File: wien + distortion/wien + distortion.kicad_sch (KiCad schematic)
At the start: 46 parts, among them J1 INPUT, J1 OUTPUT, J2 OUTPUT, J2 PWR switch, J5 Conn_01x01_Pin, U1 NE5532, U4 NE5532, U5 NE5532

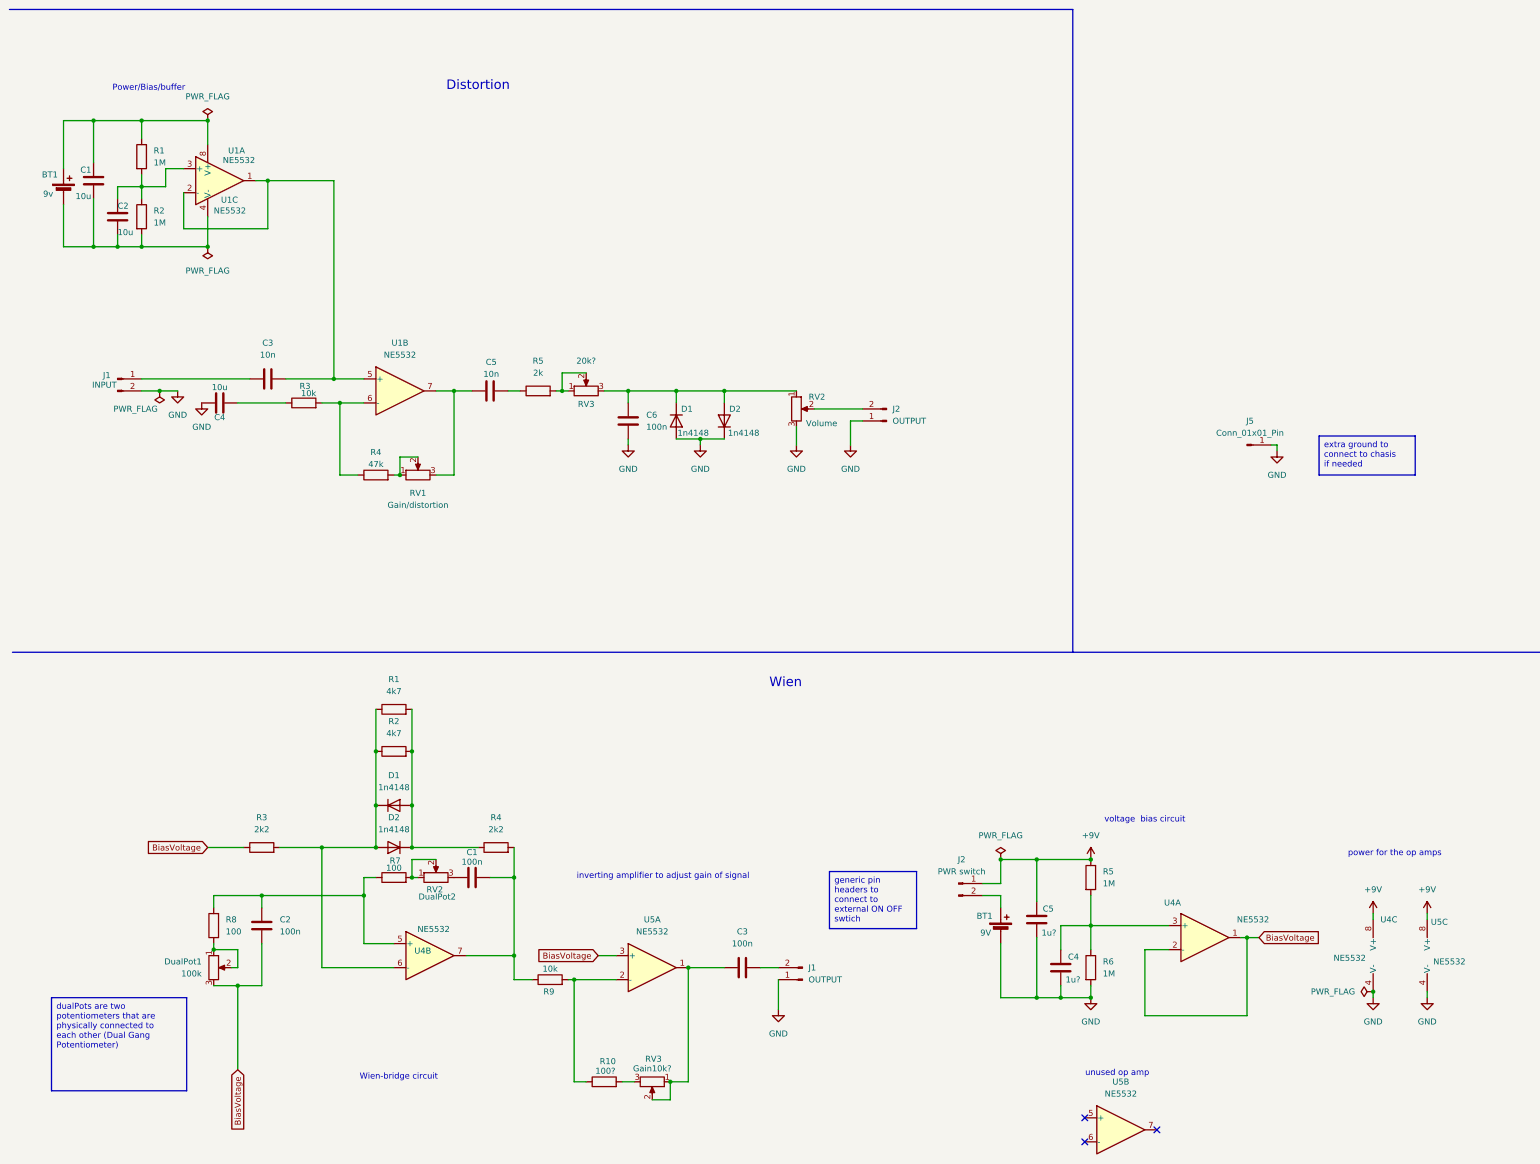
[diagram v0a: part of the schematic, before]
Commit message: decided to use one power supply for both circuits so redid the pcb to reflect that
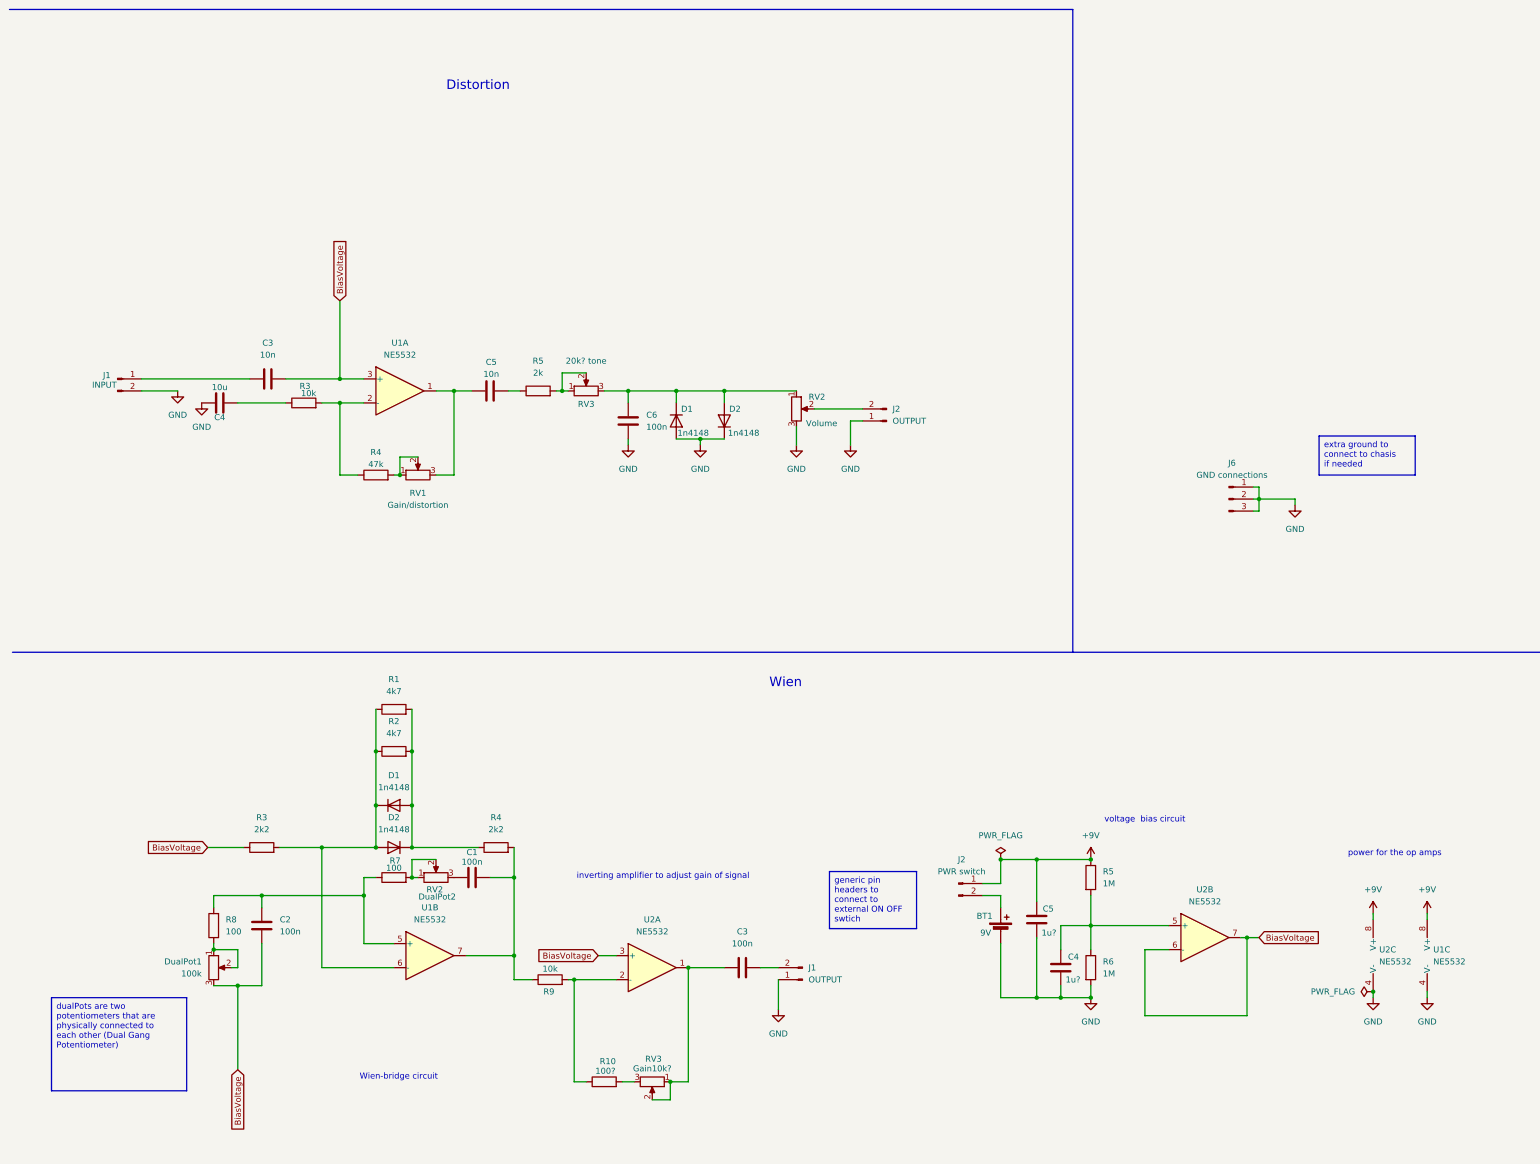
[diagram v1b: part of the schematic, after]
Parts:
- removed BT1: 9v, Connector_PinHeader_2.54mm:PinHeader_1x02_P2.54mm_Vertical, symbol Device:Battery_Cell
- removed C1, C2: 10u, Capacitor_SMD:C_0603_1608Metric_Pad1.08x0.95mm_HandSolder, symbol Device:C
- removed J5: Conn_01x01_Pin, Connector_PinHeader_2.54mm:PinHeader_1x01_P2.54mm_Vertical, symbol Connector:Conn_01x01_Pin
- removed R1, R2: 1M, Resistor_SMD:R_0603_1608Metric_Pad0.98x0.95mm_HandSolder, symbol Device:R
- removed U4, U5: NE5532, Package_DIP:DIP-8_W7.62mm, symbol Amplifier_Operational:NE5532
- added J6: GND connections, Connector_PinHeader_2.54mm:PinHeader_1x03_P2.54mm_Vertical, symbol Connector:Conn_01x03_Pin
- added U2: NE5532, Package_DIP:DIP-8_W7.62mm_LongPads, symbol Amplifier_Operational:NE5532
- RV3: value 20k? -> 20k? tone
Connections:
- net +9V: now also U1.8 (V+), U2.8 (V+)
- net BiasVoltage: now also C3.2, U1.3 (+), U2.3 (+), U2.6 (-), U2.7
- net GND: now also U1.4 (V-), J6.1 (Pin_1), J6.2 (Pin_2), J6.3 (Pin_3), U2.4 (V-)
- net at D1.1 (K), D2.2 (A), R1.1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: now also U1.6 (-)
- net at R4.2, R9.1: now also C1.1, U1.7; no longer C1.2
- net at R10.1, R9.2: now also U2.2 (-)
- net at C2.1, R7.1, R8.2: now also U1.5 (+)
- net at C3.1, RV3.1, RV3.2: now also U2.1
- net at RV2.3: now also C1.2; no longer C1.1
- net at C4.1, R5.2, R6.1: now also U2.5 (+)
- net at R3.2, R4.1: now also U1.2 (-); no longer U1.6 (-)
- net at C5.1, RV1.3: now also U1.1; no longer U1.7
- no-connect marks 3 -> 0
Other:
- note removed: "Power/Bias/buffer"
- note removed: "unused op amp"
- moved on the sheet: C1

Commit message: changed diodes to sod-123 package and changed pcb accordingly and create gerber,drill, pos,and BOM list for manufacturing
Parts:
- D1, D2: footprint Diode_SMD:D_0603_1608Metric_Pad1.05x0.95mm_HandSolder -> Diode_SMD:D_SOD-123
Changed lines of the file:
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@@
 			)
 		)
-		(property "Footprint" "Diode_SMD:D_0603_1608Metric_Pad1.05x0.95mm_HandSolder"
+		(property "Footprint" "Diode_SMD:D_SOD-123"
 			(at 152.4 123.19 0)
 			(effects
@@
 			)
 		)
-		(property "Footprint" "Diode_SMD:D_0603_1608Metric_Pad1.05x0.95mm_HandSolder"
+		(property "Footprint" "Diode_SMD:D_SOD-123"
 			(at 162.56 123.19 0)
 			(effects

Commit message: redid the manufacturing files since i had the wrong diode foot print
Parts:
- D1, D2: footprint Diode_SMD:D_0603_1608Metric_Pad1.05x0.95mm_HandSolder -> Diode_SMD:D_SOD-123
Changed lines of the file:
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@@
 			)
 		)
-		(property "Footprint" "Diode_SMD:D_0603_1608Metric_Pad1.05x0.95mm_HandSolder"
+		(property "Footprint" "Diode_SMD:D_SOD-123"
 			(at 92.71 213.36 0)
 			(effects
@@
 			)
 		)
-		(property "Footprint" "Diode_SMD:D_0603_1608Metric_Pad1.05x0.95mm_HandSolder"
+		(property "Footprint" "Diode_SMD:D_SOD-123"
 			(at 92.71 204.47 0)
 			(effects
